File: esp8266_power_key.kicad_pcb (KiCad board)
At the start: 2 copper layers, 25 parts, among them P1 CONN_01X06, P2 CONN_01X06, Q1 Q_PMOS_GDS, Q2 Q_PMOS_GDS, Q3 BC849, Q4 BC849, U1 ESP-01v090, U2 LP2988AIMX-3.3/NOPB

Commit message: 4 channel version
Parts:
- removed R1, R8: R, Resistors_SMD:R_1206
- removed the R2 at (29.0, 33.7)
- removed the R2 at (29.1, 33.7)
- added Q5: BC849, TO_SOT_Packages_SMD:SOT-23, B.Cu at (27.3, 54.6)
- added Q6: BC849, TO_SOT_Packages_SMD:SOT-23, B.Cu at (42.2, 33.5)
- added Q7: Q_PMOS_GDS, TO_SOT_Packages_SMD:TO-252-2Lead, B.Cu at (77.7, 54.9)
- added Q8: Q_PMOS_GDS, TO_SOT_Packages_SMD:TO-252-2Lead, B.Cu at (54.2, 38.6)
- added R12: R, Resistors_SMD:R_1206, B.Cu at (26.4, 47.2)
- added R13: R, Resistors_SMD:R_1206, B.Cu at (41.1, 37.1)
- added R14: R, Resistors_SMD:R_1206, B.Cu at (76.8, 61.0)
- added R15: R, Resistors_SMD:R_1206, B.Cu at (46.7, 31.5)
- added R2: R, Resistors_SMD:R_1206, B.Cu at (29.0, 32.0)
- P1: value CONN_01X06 -> CONN_01X05; footprint Connect:bornier6 -> Connect:bornier5
- P2: value CONN_01X06 -> CONN_01X05; footprint Connect:PINHEAD1-6 -> Connect:bornier5
- moved R4 24.6 mm to (66.5, 47.2), turned to 90 degrees
- moved P1 24.0 mm to (64.8, 25.4), turned to 0 degrees
- moved D1 21.8 mm to (43.2, 52.1)
- moved Q1 19.4 mm to (65.4, 39.4), turned to 180 degrees
- moved R5 16.4 mm to (71.1, 47.2)
- moved C2 16.1 mm to (47.0, 41.9), turned to 270 degrees
- moved L1 15.3 mm to (47.6, 52.1), turned to 270 degrees
- moved Q4 14.3 mm to (32.4, 54.6), turned to 270 degrees
- moved R6 12.9 mm to (62.1, 54.7), turned to 90 degrees
- moved C3 10.9 mm to (51.0, 51.7), turned to 90 degrees
- moved U2 9.90 mm to (56.2, 53.9), turned to 90 degrees
- moved Q3 7.71 mm to (36.8, 54.6), turned to 270 degrees
- moved C1 7.50 mm to (59.7, 44.5), turned to 180 degrees
- moved Q2 7.29 mm to (73.2, 39.6), turned to 180 degrees
- moved P2 7.04 mm to (39.4, 25.4), turned to 0 degrees
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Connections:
- P1 pad 1: GND -> Net-(P1-Pad1)
- P1 pad 2: GND -> Net-(C1-Pad1)
- P1 pad 3: GND -> Net-(P1-Pad3)
- P1 pad 5: Net-(C1-Pad1) -> Net-(P1-Pad5)
- P2 pad 1: Net-(C2-Pad2) -> GND
- P2 pad 2: Net-(C2-Pad2) -> GND
- P2 pad 3: Net-(P2-Pad3) -> GND
- Q1 pad 2: Net-(P1-Pad6) -> Net-(P1-Pad3)
- U1 pad 1: Net-(P2-Pad3) -> Net-(R13-Pad1)
- U1 pad 8: Net-(P2-Pad6) -> Net-(R12-Pad1)
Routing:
- net Net-(Q5-Pad3): track 0.00 -> 51.6 mm
- net Net-(C1-Pad1): track 55.9 -> 90.3 mm
- net Net-(Q3-Pad3): track 8.80 -> 40.5 mm
- net GND: track 131.6 -> 104.3 mm
- net Net-(P1-Pad5): track 0.00 -> 26.3 mm
- net Net-(Q4-Pad3): track 25.2 -> 49.7 mm
- net Net-(P2-Pad6): track 21.3 -> 0.00 mm
- net Net-(Q2-Pad1): track 27.9 -> 8.21 mm
- net Net-(Q8-Pad1): track 0.00 -> 14.6 mm
- net Net-(P2-Pad3): track 13.8 -> 0.00 mm
- net Net-(C2-Pad2): track 71.8 -> 60.6 mm
- net Net-(P1-Pad3): track 0.00 -> 8.78 mm
- net Net-(P1-Pad1): track 0.00 -> 8.09 mm
- net Net-(P1-Pad6): track 7.78 -> 0.00 mm
- net Net-(Q7-Pad1): track 0.00 -> 7.45 mm
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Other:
- net class pwr added: clearance 0.2, trace_width 1.5, via_dia 0.6, via_drill 0.4

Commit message: moved corners
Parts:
- added R1: R, Resistors_SMD:R_1206, B.Cu at (40.1, 37.6)
- moved R14 37.4 mm to (39.8, 55.9), turned to 270 degrees
- moved P2 22.7 mm to (24.6, 42.7), turned to 90 degrees
- moved Q7 14.9 mm to (63.5, 50.5), turned to 90 degrees
- moved R4 14.0 mm to (79.5, 41.9), turned to 180 degrees
- moved R3 10.7 mm to (38.9, 23.7), turned to 0 degrees
- moved U1 10.5 mm to (39.9, 27.3)
- moved R9 9.44 mm to (38.9, 42.9), turned to 270 degrees
- moved R2 9.38 mm to (33.4, 23.7), turned to 180 degrees
- moved R13 7.40 mm to (42.7, 29.8), turned to 270 degrees
- moved Q3 6.76 mm to (39.8, 48.5)
- moved R6 6.66 mm to (56.4, 58.2), turned to 0 degrees
- moved R12 5.93 mm to (30.5, 42.9)
- moved D1 5.80 mm to (45.5, 57.4), turned to 180 degrees
- moved Q5 5.50 mm to (31.5, 58.2)
- moved P1 5.09 mm to (59.7, 25.1)
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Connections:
- R14 pad 1: Net-(Q5-Pad3) -> Net-(Q3-Pad3)
- R4 pad 1: Net-(Q3-Pad3) -> Net-(Q5-Pad3)
- R9 pad 1: Net-(R9-Pad1) -> Net-(R1-Pad2)
- U1 pad 4: Net-(R10-Pad1) -> Net-(R1-Pad2)
- U1 pad 6: Net-(R9-Pad1) -> Net-(R10-Pad1)
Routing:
- net Net-(Q3-Pad3): track 40.5 -> 4.92 mm
- net Net-(Q7-Pad1): track 7.45 -> 31.9 mm
- net Net-(C2-Pad2): track 60.6 -> 78.4 mm
- net Net-(C1-Pad1): track 90.3 -> 74.2 mm
- net Net-(P1-Pad5): track 26.3 -> 42.2 mm
- net Net-(R1-Pad2): track 0.00 -> 14.1 mm
- net Net-(Q5-Pad3): track 51.6 -> 65.3 mm
- net Net-(R9-Pad1): track 13.7 -> 0.00 mm
- net GND: track 104.3 -> 113.2 mm
- net Net-(Q1-Pad1): track 21.3 -> 12.6 mm
- net Net-(Q5-Pad1): track 4.94 -> 12.8 mm
- net Net-(R10-Pad1): track 5.79 -> 11.7 mm
- net Net-(Q4-Pad3): track 49.7 -> 55.0 mm
- net Net-(Q8-Pad1): track 14.6 -> 9.35 mm
- net Net-(R12-Pad1): track 7.16 -> 12.4 mm
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
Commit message: Rev 2.0
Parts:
- removed C1: CP, Capacitors_ThroughHole:C_Radial_D8_L13_P3.8
- removed C2: CP, Capacitors_Tantalum_SMD:Tantalum_Case-D_EIA-7343-31_Hand
- removed D1: D, Diodes_SMD:SMA_Standard
- removed P2: CONN_01X05, Connect:bornier5
- removed Q7, Q8: Q_PMOS_GDS, TO_SOT_Packages_SMD:TO-252-2Lead
- removed R13, R14, R15: R, Resistors_SMD:R_1206
- added P3: CONN_01X06, Connect:bornier6, F.Cu at (102.9, 63.5)
- added R8: R, Resistors_SMD:R_1206, B.Cu at (80.5, 76.5)
- P1: value CONN_01X05 -> CONN_01X02; footprint Connect:bornier5 -> Connect:bornier2
- Q1, Q2: value Q_PMOS_GDS -> Q_NMOS_GDS
- Q3: value BC849 -> Q_NMOS_GDS; footprint TO_SOT_Packages_SMD:SOT-23 -> TO_SOT_Packages_SMD:TO-252-2Lead
- moved R9 79.9 mm to (107.7, 83.6)
- moved R2 68.6 mm to (69.7, 81.9)
- moved R12 68.3 mm to (90.1, 76.3), turned to 180 degrees
- moved Q3 64.3 mm to (96.5, 78.7), turned to 180 degrees
- moved R3 63.6 mm to (69.7, 79.4), turned to 180 degrees
- moved Q1 62.6 mm to (114.3, 78.7)
- moved R10 62.6 mm to (80.3, 86.2), turned to 180 degrees
- moved Q4 60.3 mm to (84.6, 85.4), turned to 0 degrees
- moved Q6 60.1 mm to (84.6, 76.7)
- moved U1 60.0 mm to (73.7, 76.8), turned to 0 degrees
- moved Q5 57.8 mm to (84.6, 81.0), turned to 0 degrees
- moved R4 55.8 mm to (116.6, 83.6), turned to 270 degrees
- moved R1 51.2 mm to (76.3, 73.9)
- moved Q2 47.1 mm to (105.4, 78.7)
- moved P1 44.6 mm to (82.5, 63.5), turned to 180 degrees
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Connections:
- L1 pad 1: Net-(C2-Pad2) -> +3V3
- P1 pad 1: Net-(P1-Pad1) -> +36V
- P1 pad 2: Net-(C1-Pad1) -> GND
- Q1 pad 2: Net-(P1-Pad3) -> Net-(P3-Pad5)
- Q1 pad 3: Net-(C1-Pad1) -> +36V
- Q2 pad 2: Net-(P1-Pad4) -> Net-(P3-Pad3)
- Q2 pad 3: Net-(C1-Pad1) -> +36V
- Q3 pad 2: Net-(C2-Pad2) -> Net-(P3-Pad1)
- Q3 pad 3: Net-(Q3-Pad3) -> +36V
- Q4 pad 2: Net-(C2-Pad2) -> GND
- Q5 pad 2: Net-(C2-Pad2) -> GND
- Q6 pad 2: Net-(C2-Pad2) -> GND
- R1 pad 1: GND -> Net-(Q4-Pad1)
- R10 pad 1: Net-(R10-Pad1) -> Net-(Q6-Pad1)
- R10 pad 2: Net-(Q4-Pad1) -> Net-(R10-Pad2)
- R12 pad 1: Net-(R12-Pad1) -> Net-(Q3-Pad1)
- R12 pad 2: Net-(Q5-Pad1) -> Net-(Q6-Pad3)
- R4 pad 1: Net-(Q5-Pad3) -> Net-(Q1-Pad1)
- R4 pad 2: Net-(Q1-Pad1) -> Net-(Q4-Pad3)
- R5 pad 1: Net-(Q4-Pad3) -> Net-(Q5-Pad1)
- R5 pad 2: Net-(Q2-Pad1) -> Net-(R5-Pad2)
- R6 pad 2: Net-(C1-Pad1) -> +36V
- R7 pad 2: Net-(C2-Pad2) -> +3V3
- R9 pad 1: Net-(R1-Pad2) -> Net-(Q2-Pad1)
- R9 pad 2: Net-(Q3-Pad1) -> Net-(Q5-Pad3)
- U1 pad 1: Net-(R13-Pad1) -> Net-(R1-Pad2)
- U1 pad 2: Net-(C2-Pad2) -> GND
- U1 pad 4: Net-(R1-Pad2) -> Net-(R8-Pad2)
- U1 pad 6: Net-(R10-Pad1) -> Net-(R5-Pad2)
- U1 pad 7: GND -> +3V3
- U1 pad 8: Net-(R12-Pad1) -> Net-(R10-Pad2)
- U2 pad 6: Net-(C1-Pad1) -> +36V
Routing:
- net GND: track 113.2 -> 0.00 mm
- net Net-(C2-Pad2): track 78.4 -> 0.00 mm
- net Net-(C1-Pad1): track 74.2 -> 0.00 mm
- net Net-(P1-Pad5): track 42.2 -> 0.00 mm
- net Net-(Q5-Pad3): track 65.3 -> 25.4 mm
- net +36V: track 0.00 -> 36.8 mm
- net Net-(Q7-Pad1): track 31.9 -> 0.00 mm
- net Net-(Q4-Pad3): track 55.0 -> 32.9 mm
- net Net-(P1-Pad4): track 16.4 -> 0.00 mm
- net Net-(R6-Pad1): track 14.4 -> 0.00 mm
- net Net-(R1-Pad2): track 14.1 -> 0.00 mm
- net Net-(Q5-Pad1): track 12.8 -> 0.00 mm
- net Net-(Q1-Pad1): track 12.6 -> 0.00 mm
- net Net-(R12-Pad1): track 12.4 -> 0.00 mm
- net Net-(R10-Pad1): track 11.7 -> 0.00 mm
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- removed copper zone on B.Cu, net GND

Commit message: resaved
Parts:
- Q1: value Q_NMOS_GDS -> Q_PMOS_GDS
- Q2, Q3: value Q_NMOS_GDS -> Q_PMOS_GDS; moved to F.Cu
- moved Q2 131.6 mm to (0.00, 0.00), turned to 0 degrees
- moved Q3 124.6 mm to (0.00, 0.00), turned to 0 degrees
- moved R4 3.23 mm to (117.0, 86.8), turned to 180 degrees
- moved Q1 2.59 mm to (112.0, 77.6)
- moved R9 1.70 mm to (108.5, 85.1), turned to 180 degrees
- moved P3 1.58 mm to (104.4, 63.4)
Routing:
- net +36V: track 36.8 -> 0.00 mm
- net Net-(Q4-Pad3): track 32.9 -> 0.00 mm
- net Net-(Q5-Pad3): track 25.4 -> 0.00 mm

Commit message: last save
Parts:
- removed Q3: Q_PMOS_GDS, TO_SOT_Packages_SMD:TO-252-2Lead
- removed Q5: BC849, TO_SOT_Packages_SMD:SOT-23
- added C1: CP, Capacitors_ThroughHole:CP_Radial_D8.0mm_P3.80mm, F.Cu at (77.2, 63.0)
- added C2: CP, Capacitors_ThroughHole:CP_Radial_Tantal_D5.0mm_P2.50mm, F.Cu at (73.2, 81.0)
- added C4: C, Capacitors_SMD:C_1206, B.Cu at (103.1, 71.4)
- added C5: CP, Capacitors_ThroughHole:CP_Radial_D8.0mm_P3.80mm, F.Cu at (105.7, 73.7)
- added C6: C, Capacitors_SMD:C_1206, B.Cu at (118.9, 69.7)
- added C7: CP, Capacitors_ThroughHole:CP_Radial_D8.0mm_P3.80mm, F.Cu at (116.2, 73.5)
- added D1: D, Diodes_SMD:D_SMA_Handsoldering, B.Cu at (67.3, 80.3)
- added P2: CONN_01X02, Connect:bornier2, F.Cu at (97.4, 63.5)
- added R13: R, Resistors_SMD:R_1206, B.Cu at (84.6, 78.5)
- added R14: R, Resistors_SMD:R_1206, B.Cu at (88.1, 67.3)
- P3: value CONN_01X06 -> CONN_01X02; footprint Connect:bornier6 -> Connect:bornier2
- Q1: value Q_PMOS_GDS -> Q_NMOS_SDG
- Q2: value Q_PMOS_GDS -> Q_NMOS_SDG; moved to B.Cu
- moved Q2 134.1 mm to (110.7, 75.6), turned to 180 degrees
- moved R10 39.1 mm to (118.7, 79.2), turned to 270 degrees
- moved Q6 30.1 mm to (114.6, 79.5), turned to 180 degrees
- moved R5 29.4 mm to (103.4, 63.8), turned to 270 degrees
- moved R4 27.1 mm to (92.1, 76.2)
- moved R9 22.7 mm to (117.2, 64.1), turned to 0 degrees
- moved C3 18.5 mm to (65.3, 75.9), turned to 270 degrees
- moved R12 16.0 mm to (105.9, 78.2), turned to 270 degrees
- moved L1 14.2 mm to (70.4, 75.7)
- moved Q1 14.0 mm to (98.0, 76.2)
- moved Q4 13.1 mm to (87.4, 72.6)
- moved R3 9.63 mm to (75.4, 71.6), turned to 90 degrees
- moved R8 8.18 mm to (88.4, 78.5), turned to 90 degrees
- moved R2 7.99 mm to (75.4, 76.3), turned to 90 degrees
- moved R1 7.89 mm to (83.8, 71.6), turned to 90 degrees
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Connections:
- P3 pad 1: Net-(P3-Pad1) -> Net-(C6-Pad2)
- Q1 pad 2: Net-(P3-Pad5) -> Net-(C4-Pad2)
- Q1 pad 3: +36V -> Net-(Q1-Pad3)
- Q2 pad 1: Net-(Q2-Pad1) -> Net-(Q1-Pad1)
- Q2 pad 2: Net-(P3-Pad3) -> Net-(C6-Pad2)
- Q2 pad 3: +36V -> Net-(Q2-Pad3)
- R12 pad 1: Net-(Q3-Pad1) -> Net-(Q2-Pad3)
- R2 pad 2: GND -> +3V3
- R3 pad 2: GND -> +3V3
- R4 pad 1: Net-(Q1-Pad1) -> Net-(Q1-Pad3)
- R5 pad 1: Net-(Q5-Pad1) -> GND
- R5 pad 2: Net-(R5-Pad2) -> Net-(C4-Pad1)
- R9 pad 1: Net-(Q2-Pad1) -> GND
- U1 pad 6: Net-(R5-Pad2) -> Net-(R13-Pad2)
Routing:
- net GND: track 0.00 -> 215.8 mm
- net Net-(R10-Pad2): track 0.00 -> 40.1 mm
- net Net-(Q1-Pad1): track 0.00 -> 39.3 mm
- net +3V3: track 0.00 -> 33.5 mm
- net +36V: track 0.00 -> 28.3 mm
- net Net-(C6-Pad2): track 0.00 -> 18.4 mm
- net Net-(R6-Pad1): track 0.00 -> 17.7 mm
- net Net-(C4-Pad2): track 0.00 -> 16.9 mm
- net Net-(C6-Pad1): track 0.00 -> 10.2 mm
- net Net-(R11-Pad2): track 0.00 -> 9.50 mm
- net Net-(R8-Pad2): track 0.00 -> 9.45 mm
- net Net-(D1-Pad1): track 0.00 -> 8.73 mm
- net Net-(R1-Pad2): track 0.00 -> 8.16 mm
- net Net-(C4-Pad1): track 0.00 -> 8.15 mm
- net Net-(Q6-Pad3): track 0.00 -> 7.71 mm
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- added copper zone on B.Cu, net GND
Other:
- board outline added: 59.7 x 23.2 mm

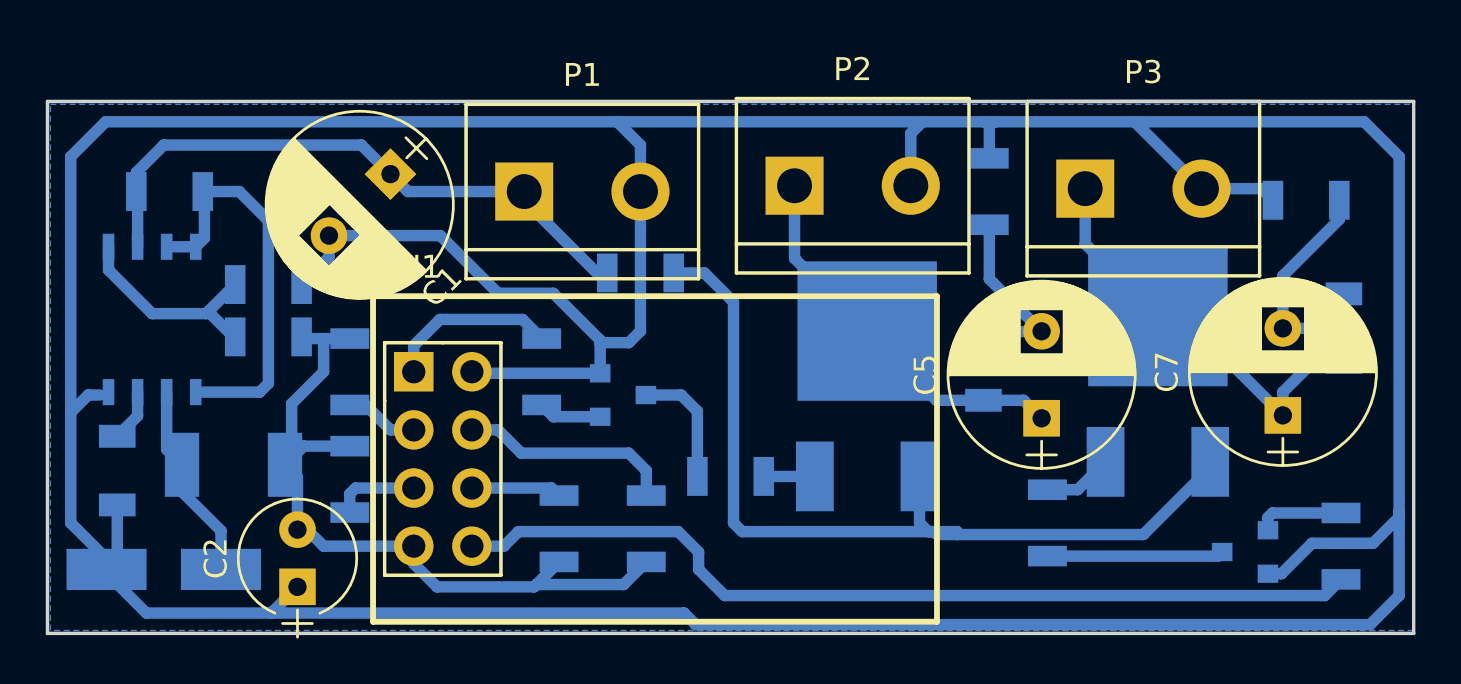
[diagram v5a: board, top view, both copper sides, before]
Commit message: topology fix
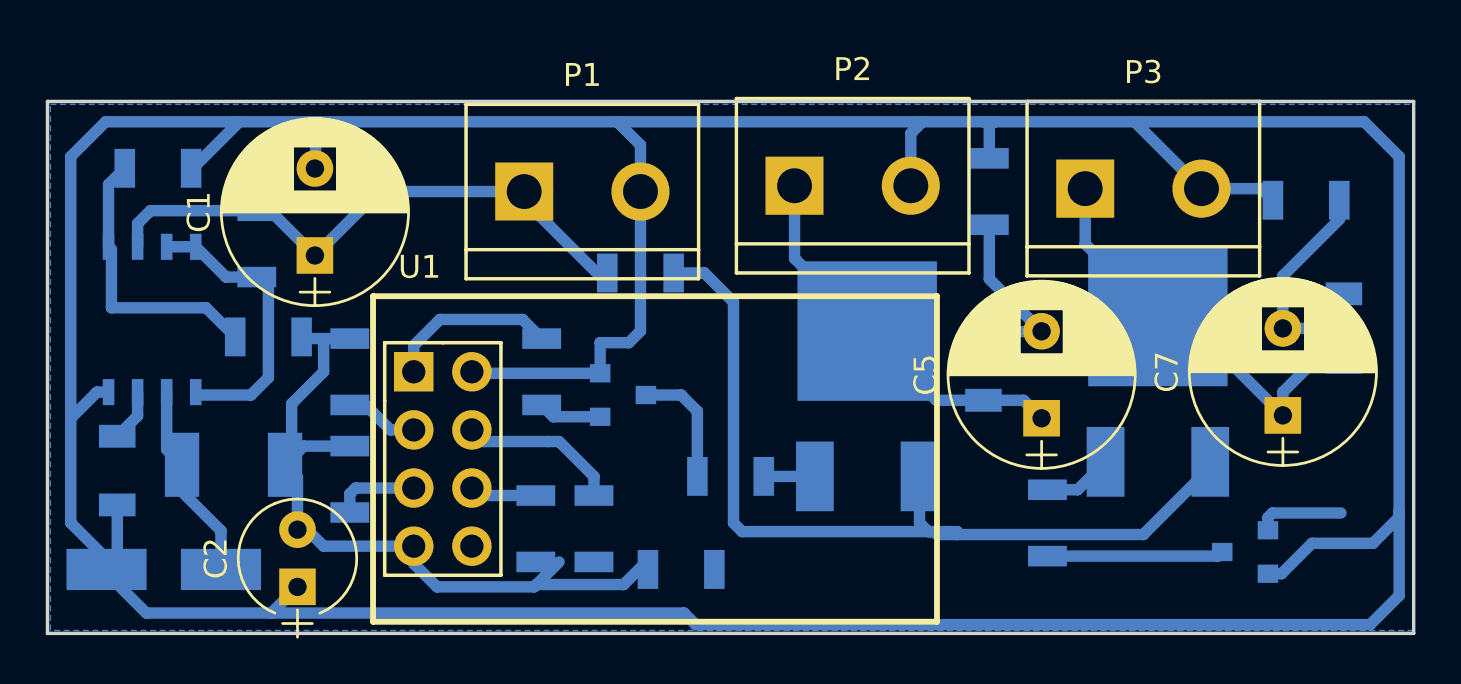
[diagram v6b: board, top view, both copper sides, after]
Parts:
- moved R10 28.8 mm to (89.9, 80.3), turned to 180 degrees
- moved R11 7.01 mm to (67.1, 62.7)
- moved C1 4.85 mm to (73.9, 66.5), turned to 90 degrees
- moved R6 4.44 mm to (71.4, 66.0), turned to 90 degrees
- moved R8 2.29 mm to (86.1, 78.5)
- moved R13 1.02 mm to (83.6, 78.5)
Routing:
- net Net-(R10-Pad2): track 40.1 -> 1.40 mm
- net GND: track 215.8 -> 204.7 mm
- net Net-(R6-Pad1): track 17.7 -> 12.6 mm
- net Net-(R11-Pad2): track 9.50 -> 12.5 mm
- net Net-(R8-Pad2): track 9.45 -> 7.01 mm
- net +36V: track 28.3 -> 26.6 mm
- net +3V3: track 33.5 -> 32.1 mm
- net Net-(R13-Pad2): track 3.95 -> 2.93 mm

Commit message: minor fixes
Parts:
- R14: footprint Resistors_SMD:R_1206 -> Resistors_SMD:R_1206_HandSoldering
- moved Q6 22.2 mm to (92.3, 80.0), turned to 0 degrees
- moved R14 5.46 mm to (93.1, 69.6), turned to 90 degrees
- moved R1 3.15 mm to (81.8, 69.2), turned to 180 degrees
- moved C2 2.57 mm to (75.3, 79.6), turned to 120 degrees
- moved C6 2.29 mm to (118.9, 72.0)
- moved R4 2.27 mm to (93.1, 74.2)
- moved Q4 1.65 mm to (87.4, 71.0), turned to 270 degrees
- moved Q1 1.42 mm to (99.3, 75.6)
- moved D1 1.28 mm to (68.6, 80.4), turned to 0 degrees
- moved R2 1.15 mm to (75.6, 75.2), turned to 180 degrees
- moved U1 1.05 mm to (79.2, 71.9)
- moved R3 1.02 mm to (75.6, 72.6), turned to 180 degrees
- moved C4 0.97 mm to (104.0, 71.0)
- moved R9 0.92 mm to (116.5, 63.6), turned to 270 degrees
- moved R10 0.90 mm to (89.3, 79.6), turned to 90 degrees
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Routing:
- net GND: track 204.7 -> 1.93 mm
- net Net-(R10-Pad2): track 1.40 -> 10.5 mm
- net Net-(Q1-Pad1): track 39.3 -> 30.5 mm
- net +36V: track 26.6 -> 33.9 mm
- net Net-(Q6-Pad3): track 7.71 -> 14.6 mm
- net Net-(R1-Pad2): track 8.16 -> 3.12 mm
- net Net-(R6-Pad1): track 12.6 -> 16.4 mm
- net Net-(C6-Pad1): track 10.2 -> 7.70 mm
- net +3V3: track 32.1 -> 33.9 mm
- net Net-(Q6-Pad1): track 3.83 -> 2.18 mm
- net Net-(C6-Pad2): track 18.4 -> 16.9 mm
- net Net-(R2-Pad1): track 3.97 -> 2.76 mm
- net Net-(R11-Pad2): track 12.5 -> 11.4 mm
- net Net-(R8-Pad2): track 7.01 -> 5.97 mm
- net Net-(Q1-Pad3): track 2.23 -> 3.25 mm
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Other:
- net class Default: trace_width 0.5 -> 0.6
- net class pwr: trace_width 1.5 -> 0.6
